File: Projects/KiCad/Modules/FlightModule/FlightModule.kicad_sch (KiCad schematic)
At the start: 66 parts, among them J1 Conn_01x08, J2 Conn_01x02_Pin, J3 Conn_01x02_Pin, J4 Conn_01x02_Pin, J5 Conn_01x02_Pin, J6 Conn_01x02_Pin, Q1 Q_NPN_BEC, Q2 Q_NPN_BEC, SW1 SW_DIP_x02, U1 MCP2562-E-P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

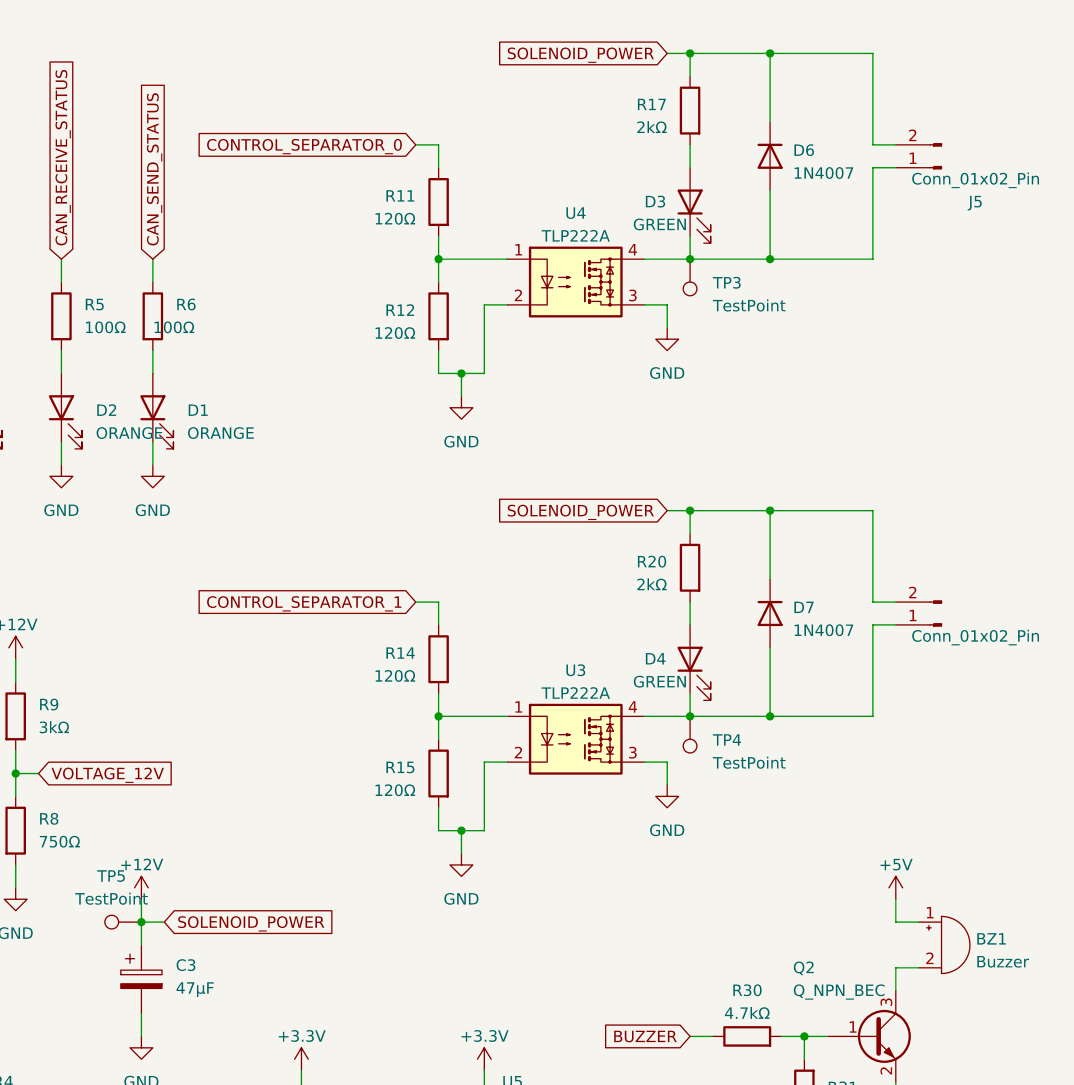
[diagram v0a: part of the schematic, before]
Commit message: 電磁弁制御のフォトカプラの位置を修正
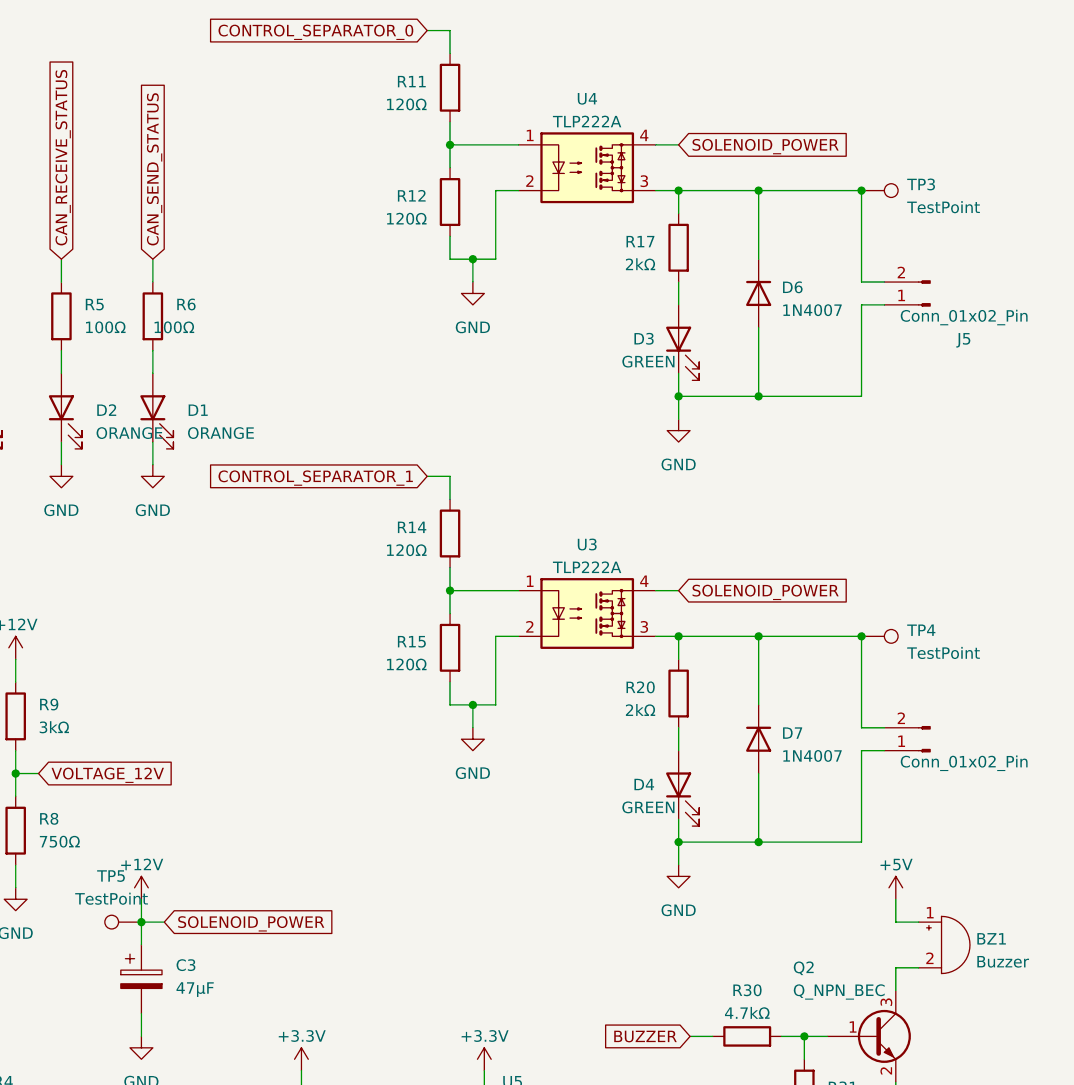
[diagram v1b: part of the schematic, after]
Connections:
- net +12V: now also U3.4, U4.4; no longer D6.1 (K), D7.1 (K), J4.2 (Pin_2), J5.2 (Pin_2), R17.1, R20.1
- net GND: now also D3.1 (K), D4.1 (K), D6.2 (A), D7.2 (A), J4.1 (Pin_1), J5.1 (Pin_1); no longer U3.3, U4.3
- new net: D6.1 (K), J5.2 (Pin_2), R17.1, TP3.1, U4.3
- new net: D7.1 (K), J4.2 (Pin_2), R20.1, TP4.1, U3.3
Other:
- moved on the sheet: D3, D4, D6, D7, J5, R14, R15, R17, R20, TP3, TP4, U3

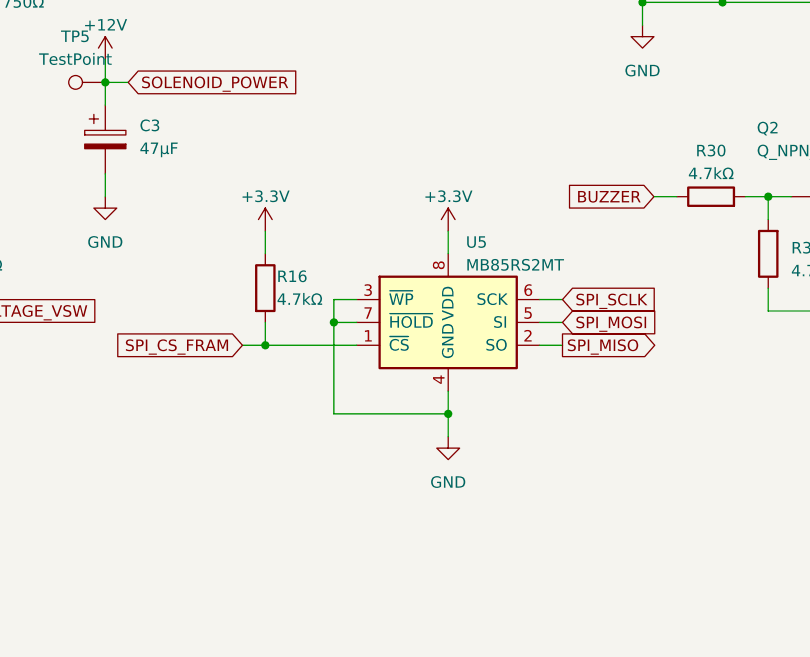
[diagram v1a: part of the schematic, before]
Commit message: FRAMのWPとHOLDをHIGHに固定
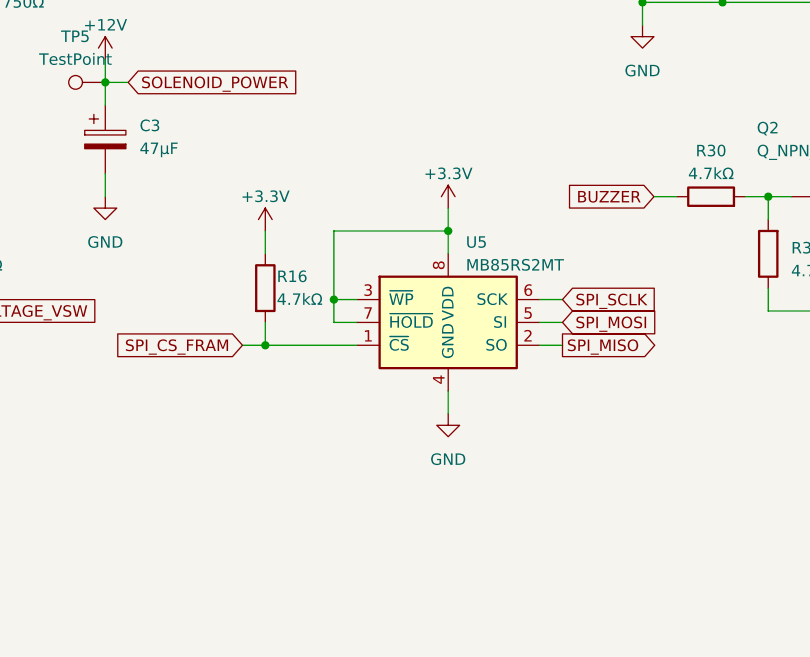
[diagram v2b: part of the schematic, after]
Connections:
- net +3.3V: now also U5.3 (~{WP}), U5.7 (~{HOLD})
- net GND: no longer U5.3 (~{WP}), U5.7 (~{HOLD})
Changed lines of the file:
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@@
   (junction (at 26.67 36.83) (diameter 0) (color 0 0 0 0)
   )
+  (junction (at 220.98 133.35) (diameter 0) (color 0 0 0 0)
+  )
   (junction (at 251.46 107.95) (diameter 0) (color 0 0 0 0)
   )
@@
   (junction (at 242.57 85.09) (diameter 0) (color 0 0 0 0)
   )
-  (junction (at 208.28 143.51) (diameter 0) (color 0 0 0 0)
-  )
   (junction (at 34.29 87.63) (diameter 0) (color 0 0 0 0)
   )
-  (junction (at 220.98 153.67) (diameter 0) (color 0 0 0 0)
-  )
   (junction (at 74.93 49.53) (diameter 0) (color 0 0 0 0)
   )
@@
   (junction (at 161.29 180.34) (diameter 0) (color 0 0 0 0)
   )
+  (junction (at 208.28 140.97) (diameter 0) (color 0 0 0 0)
+  )
   (no_connect (at 90.17 149.86))
   (no_connect (at 38.1 139.7))
@@
     (stroke (width 0) (type default))
   )
+  (wire (pts (xy 220.98 133.35) (xy 220.98 135.89))
+    (stroke (width 0) (type default))
+  )
   (wire (pts (xy 262.89 35.56) (xy 262.89 45.72))
     (stroke (width 0) (type default))
@@
     (stroke (width 0) (type default))
   )
+  (wire (pts (xy 208.28 140.97) (xy 208.28 133.35))
+    (stroke (width 0) (type default))
+  )
   (wire (pts (xy 34.29 87.63) (xy 36.83 87.63))
     (stroke (width 0) (type default))
@@
     (stroke (width 0) (type default))
   )
-  (wire (pts (xy 220.98 153.67) (xy 220.98 156.21))
-    (stroke (width 0) (type default))
-  )
   (wire (pts (xy 231.14 143.51) (xy 233.68 143.51))
     (stroke (width 0) (type default))
@@
     (stroke (width 0) (type default))
   )
-  (wire (pts (xy 208.28 143.51) (xy 208.28 153.67))
-    (stroke (width 0) (type default))
-  )
   (wire (pts (xy 262.89 97.79) (xy 262.89 107.95))
     (stroke (width 0) (type default))
@@
     (stroke (width 0) (type default))
   )
-  (wire (pts (xy 220.98 133.35) (xy 220.98 135.89))
+  (wire (pts (xy 220.98 130.81) (xy 220.98 133.35))
     (stroke (width 0) (type default))
   )
@@
     (stroke (width 0) (type default))
   )
+  (wire (pts (xy 208.28 133.35) (xy 220.98 133.35))
+    (stroke (width 0) (type default))
+  )
   (wire (pts (xy 87.63 170.18) (xy 90.17 170.18))
     (stroke (width 0) (type default))
@@
     (stroke (width 0) (type default))
   )
-  (wire (pts (xy 208.28 153.67) (xy 220.98 153.67))
-    (stroke (width 0) (type default))
-  )
   (wire (pts (xy 217.17 30.48) (xy 217.17 33.02))
     (stroke (width 0) (type default))
@@
     )
   )
-  (symbol (lib_id "power:GND") (at 220.98 156.21 0) (unit 1)
+  (symbol (lib_id "power:GND") (at 220.98 153.67 0) (unit 1)
     (in_bom yes) (on_board yes) (dnp no) (fields_autoplaced)
-    (property "Reference" "#PWR041" (at 220.98 162.56 0)
+    (property "Reference" "#PWR041" (at 220.98 160.02 0)
       (effects (font (size 1.27 1.27)) hide)
     )
-    (property "Value" "GND" (at 220.98 161.29 0)
+    (property "Value" "GND" (at 220.98 158.75 0)
       (effects (font (size 1.27 1.27)))
     )
-    (property "Footprint" "" (at 220.98 156.21 0)
+    (property "Footprint" "" (at 220.98 153.67 0)
       (effects (font (size 1.27 1.27)) hide)
     )
-    (property "Datasheet" "" (at 220.98 156.21 0)
+    (property "Datasheet" "" (at 220.98 153.67 0)
       (effects (font (size 1.27 1.27)) hide)
     )
@@
     )
   )
-  (symbol (lib_id "power:+3.3V") (at 220.98 133.35 0) (unit 1)
+  (symbol (lib_id "power:+3.3V") (at 220.98 130.81 0) (unit 1)
     (in_bom yes) (on_board yes) (dnp no) (fields_autoplaced)
-    (property "Reference" "#PWR040" (at 220.98 137.16 0)
+    (property "Reference" "#PWR040" (at 220.98 134.62 0)
       (effects (font (size 1.27 1.27)) hide)
     )
-    (property "Value" "+3.3V" (at 220.98 129.54 0)
+    (property "Value" "+3.3V" (at 220.98 127 0)
       (effects (font (size 1.27 1.27)))
     )
-    (property "Footprint" "" (at 220.98 133.35 0)
+    (property "Footprint" "" (at 220.98 130.81 0)
       (effects (font (size 1.27 1.27)) hide)
     )
-    (property "Datasheet" "" (at 220.98 133.35 0)
+    (property "Datasheet" "" (at 220.98 130.81 0)
       (effects (font (size 1.27 1.27)) hide)
     )

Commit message: ガーバーを再生成
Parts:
- C1, C2, C4: value 0.1μF -> 0.1uF
- C3: value 47μF -> 47uF
- D1, D2: value ORANGE -> BLUE
- R1: value 120R1/4W -> 120R
- R10, R17, R20: value 2kΩ -> 2kR
- R11, R12, R14, R15: value 120Ω -> 120R
- R13, R18, R19, R21, R22: value 300Ω -> 300R
- R16, R26, R27, R30, R31: value 4.7kΩ -> 4.7kR
- R2, R7: value 820Ω -> 820R
- R23, R24: value 10kΩ -> 10kR
- R25: value 1kΩ -> 1kR
- R3: value 4.3kΩ -> 4.3kR
- R4: value 5.6kΩ -> 5.6kR
- R5, R6: value 100Ω -> 100R
- R8: value 750Ω -> 750R
- R9: value 3kΩ -> 3kR
- U3, U4: value TLP222A -> TLP241B
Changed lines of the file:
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@@
       (effects (font (size 1.27 1.27)) (justify left))
     )
-    (property "Value" "120Ω" (at 214.63 38.735 0)
+    (property "Value" "120R" (at 214.63 38.735 0)
       (effects (font (size 1.27 1.27)) (justify left))
     )
@@
       (effects (font (size 1.27 1.27)) (justify right))
     )
-    (property "Value" "ORANGE" (at 187.96 62.5474 90)
+    (property "Value" "BLUE" (at 187.96 62.5474 90)
       (effects (font (size 1.27 1.27)) (justify right))
     )
@@
       (effects (font (size 1.27 1.27)) (justify left))
     )
-    (property "Value" "120Ω" (at 214.63 75.565 0)
+    (property "Value" "120R" (at 214.63 75.565 0)
       (effects (font (size 1.27 1.27)) (justify left))
     )
@@
       (effects (font (size 1.27 1.27)) (justify right))
     )
-    (property "Value" "4.7kΩ" (at 49.53 95.885 0)
+    (property "Value" "4.7kR" (at 49.53 95.885 0)
       (effects (font (size 1.27 1.27)) (justify right))
     )
@@
       (effects (font (size 1.27 1.27)) (justify left))
     )
-    (property "Value" "120Ω" (at 214.63 88.265 0)
+    (property "Value" "120R" (at 214.63 88.265 0)
       (effects (font (size 1.27 1.27)) (justify left))
     )
@@
       (effects (font (size 1.27 1.27)) (justify left))
     )
-    (property "Value" "3kΩ" (at 171.45 95.2499 0)
+    (property "Value" "3kR" (at 171.45 95.2499 0)
       (effects (font (size 1.27 1.27)) (justify left))
     )
@@
       (effects (font (size 1.27 1.27)))
     )
-    (property "Value" "1kΩ" (at 127 96.52 90)
+    (property "Value" "1kR" (at 127 96.52 90)
       (effects (font (size 1.27 1.27)))
     )
@@
       (effects (font (size 1.27 1.27)))
     )
-    (property "Value" "4.7kΩ" (at 40.64 85.09 90)
+    (property "Value" "4.7kR" (at 40.64 85.09 90)
       (effects (font (size 1.27 1.27)))
     )
@@
       (effects (font (size 1.27 1.27)) (justify right))
     )
-    (property "Value" "4.7kΩ" (at 259.08 137.795 0)
+    (property "Value" "4.7kR" (at 259.08 137.795 0)
       (effects (font (size 1.27 1.27)) (justify right))
     )
@@
       (effects (font (size 1.27 1.27)) (justify left))
     )
-    (property "Value" "820Ω" (at 166.37 149.8599 0)
+    (property "Value" "820R" (at 166.37 149.8599 0)
       (effects (font (size 1.27 1.27)) (justify left))
     )
@@
       (effects (font (size 1.27 1.27)) (justify left))
     )
-    (property "Value" "0.1μF" (at 90.17 33.02 0)
+    (property "Value" "0.1uF" (at 90.17 33.02 0)
       (effects (font (size 1.27 1.27)) (justify left))
     )
@@
       (effects (font (size 1.27 1.27)) (justify left))
     )
-    (property "Value" "300Ω" (at 152.4 51.435 0)
+    (property "Value" "300R" (at 152.4 51.435 0)
       (effects (font (size 1.27 1.27)) (justify left))
     )
@@
       (effects (font (size 1.27 1.27)) (justify left))
     )
-    (property "Value" "4.3kΩ" (at 147.32 137.1599 0)
+    (property "Value" "4.3kR" (at 147.32 137.1599 0)
       (effects (font (size 1.27 1.27)) (justify left))
     )
@@
       (effects (font (size 1.27 1.27)) (justify left))
     )
-    (property "Value" "2kΩ" (at 240.03 43.815 0)
+    (property "Value" "2kR" (at 240.03 43.815 0)
       (effects (font (size 1.27 1.27)) (justify left))
     )
@@
       (effects (font (size 1.27 1.27)) (justify left))
     )
-    (property "Value" "300Ω" (at 132.08 51.435 0)
+    (property "Value" "300R" (at 132.08 51.435 0)
       (effects (font (size 1.27 1.27)) (justify left))
     )
@@
       (effects (font (size 1.27 1.27)))
     )
-    (property "Value" "TLP222A" (at 232.41 27.94 0)
+    (property "Value" "TLP241B" (at 232.41 27.94 0)
       (effects (font (size 1.27 1.27)))
     )
@@
       (effects (font (size 1.27 1.27)) (justify left))
     )
-    (property "Value" "10kΩ" (at 100.33 93.98 0)
+    (property "Value" "10kR" (at 100.33 93.98 0)
       (effects (font (size 1.27 1.27)) (justify left))
     )
@@
       (effects (font (size 1.27 1.27)) (justify left))
     )
-    (property "Value" "4.7kΩ" (at 201.93 140.97 0)
+    (property "Value" "4.7kR" (at 201.93 140.97 0)
       (effects (font (size 1.27 1.27)) (justify left))
     )
@@
       (effects (font (size 1.27 1.27)) (justify left))
     )
-    (property "Value" "0.1μF" (at 81.28 33.02 0)
+    (property "Value" "0.1uF" (at 81.28 33.02 0)
       (effects (font (size 1.27 1.27)) (justify left))
     )
@@
       (effects (font (size 1.27 1.27)) (justify left))
     )
-    (property "Value" "0.1μF" (at 123.19 106.68 0)
+    (property "Value" "0.1uF" (at 123.19 106.68 0)
       (effects (font (size 1.27 1.27)) (justify left))
     )
@@
       (effects (font (size 1.27 1.27)) (justify left))
     )
-    (property "Value" "300Ω" (at 142.24 51.435 0)
+    (property "Value" "300R" (at 142.24 51.435 0)
       (effects (font (size 1.27 1.27)) (justify left))
     )
@@
       (effects (font (size 1.27 1.27)) (justify left))
     )
-    (property "Value" "120Ω" (at 214.63 26.035 0)
+    (property "Value" "120R" (at 214.63 26.035 0)
       (effects (font (size 1.27 1.27)) (justify left))
     )
@@
       (effects (font (size 1.27 1.27)))
     )
-    (property "Value" "TLP222A" (at 232.41 77.47 0)
+    (property "Value" "TLP241B" (at 232.41 77.47 0)
       (effects (font (size 1.27 1.27)))
     )
@@
       (effects (font (size 1.27 1.27)) (justify left))
     )
-    (property "Value" "750Ω" (at 171.45 107.9499 0)
+    (property "Value" "750R" (at 171.45 107.9499 0)
       (effects (font (size 1.27 1.27)) (justify left))
     )
@@
       (effects (font (size 1.27 1.27)) (justify right))
     )
-    (property "Value" "ORANGE" (at 177.8 62.5474 90)
+    (property "Value" "BLUE" (at 177.8 62.5474 90)
       (effects (font (size 1.27 1.27)) (justify right))
     )
@@
       (effects (font (size 1.27 1.27)) (justify left))
     )
-    (property "Value" "820Ω" (at 147.32 149.8599 0)
+    (property "Value" "820R" (at 147.32 149.8599 0)
       (effects (font (size 1.27 1.27)) (justify left))
     )
@@
       (effects (font (size 1.27 1.27)) (justify left))
     )
-    (property "Value" "2kΩ" (at 240.03 93.345 0)
+    (property "Value" "2kR" (at 240.03 93.345 0)
       (effects (font (size 1.27 1.27)) (justify left))
     )
@@
       (effects (font (size 1.27 1.27)) (justify left))
     )
-    (property "Value" "2kΩ" (at 160.02 95.2499 0)
+    (property "Value" "2kR" (at 160.02 95.2499 0)
       (effects (font (size 1.27 1.27)) (justify left))
     )
@@
       (effects (font (size 1.27 1.27)) (justify left))
     )
-    (property "Value" "100Ω" (at 184.15 50.7999 0)
+    (property "Value" "100R" (at 184.15 50.7999 0)
       (effects (font (size 1.27 1.27)) (justify left))
     )
@@
       (effects (font (size 1.27 1.27)))
     )
-    (property "Value" "4.7kΩ" (at 250.19 127 90)
+    (property "Value" "4.7kR" (at 250.19 127 90)
       (effects (font (size 1.27 1.27)))
     )
@@
       (effects (font (size 1.27 1.27)))
     )
-    (property "Value" "10kΩ" (at 114.3 96.52 90)
+    (property "Value" "10kR" (at 114.3 96.52 90)
       (effects (font (size 1.27 1.27)))
     )
@@
       (effects (font (size 1.27 1.27)) (justify left))
     )
-    (property "Value" "100Ω" (at 176.53 50.7999 0)
+    (property "Value" "100R" (at 176.53 50.7999 0)
       (effects (font (size 1.27 1.27)) (justify left))
     )
@@
       (effects (font (size 1.27 1.27)) (justify left))
     )
-    (property "Value" "5.6kΩ" (at 166.37 137.1599 0)
+    (property "Value" "5.6kR" (at 166.37 137.1599 0)
       (effects (font (size 1.27 1.27)) (justify left))
     )
@@
       (effects (font (size 1.27 1.27)) (justify left))
     )
-    (property "Value" "47μF" (at 186.69 124.206 0)
+    (property "Value" "47uF" (at 186.69 124.206 0)
       (effects (font (size 1.27 1.27)) (justify left))
     )
@@
       (effects (font (size 1.27 1.27)) (justify left))
     )
-    (property "Value" "120R1/4W" (at 76.2 54.61 0)
+    (property "Value" "120R" (at 76.2 54.61 0)
       (effects (font (size 1.27 1.27)) (justify left))
     )
@@
       (effects (font (size 1.27 1.27)) (justify left))
     )
-    (property "Value" "300Ω" (at 31.75 95.885 0)
+    (property "Value" "300R" (at 31.75 95.885 0)
       (effects (font (size 1.27 1.27)) (justify left))
     )
@@
       (effects (font (size 1.27 1.27)) (justify left))
     )
-    (property "Value" "300Ω" (at 162.56 51.435 0)
-      (effects (font (size 1.27 1.27)) (justify left))
-    )
+    (property "Value" "300R" (at 162.56 51.435 0)
+      (effects (font (size 1.27 1.27)) (justify left))
+    )
